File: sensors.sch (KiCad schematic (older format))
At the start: 13 parts, among them Q7 IRLML2502, SW1 TL6215RF200BDT, U13 VL53L0X, U14 APDS-9960

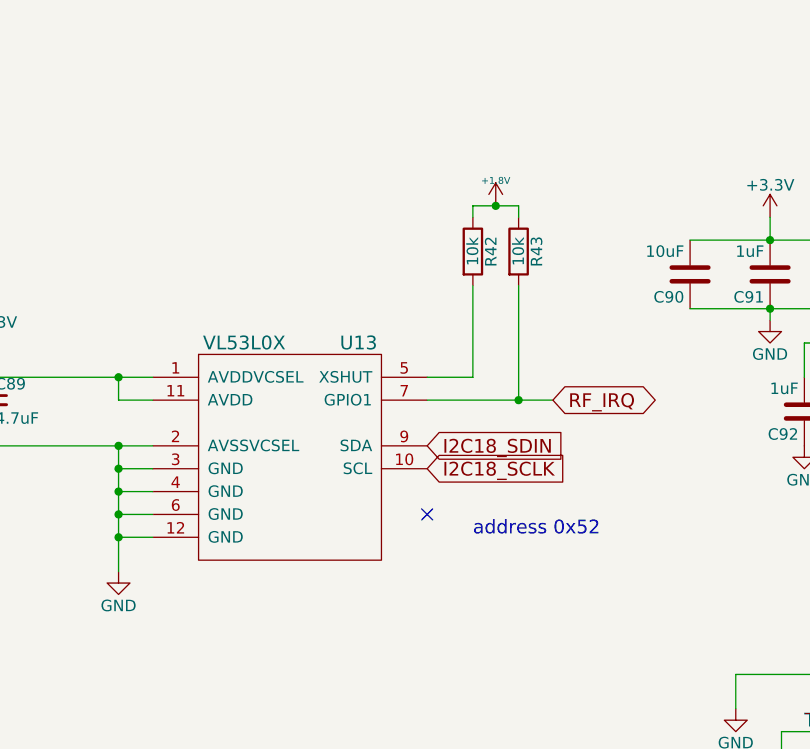
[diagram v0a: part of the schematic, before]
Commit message: added arduino header, shifted components, deleted 50pin ZIF, deleted MIDI in for fear of confusion with headphone jack
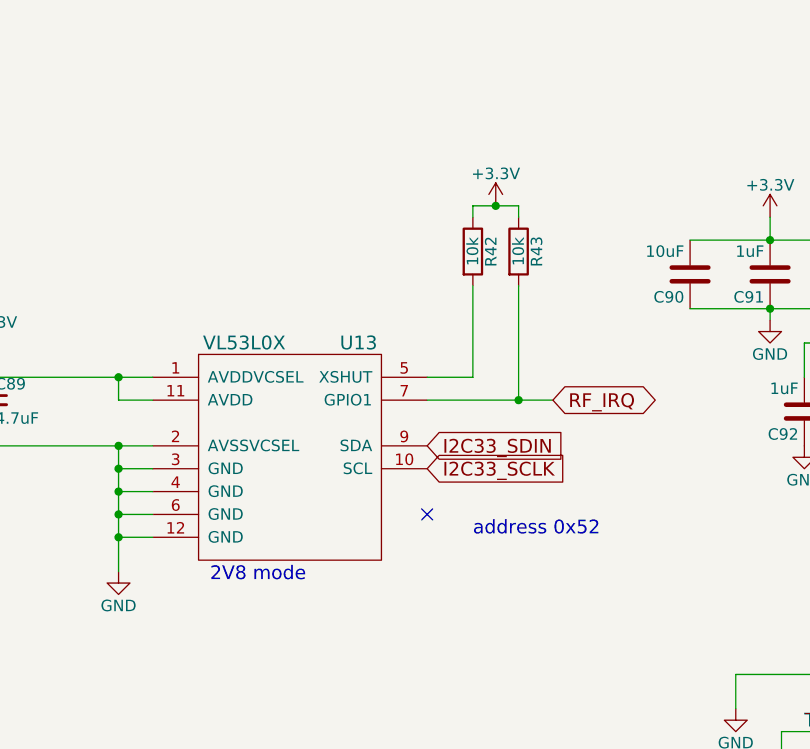
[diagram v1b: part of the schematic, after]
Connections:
- net I2C18_SCLK is gone; now on net I2C33_SCLK: U13.10 (SCL)
- net +1V8: no longer R42.1, R43.1
- net +3V3: now also R42.1, R43.1
- net I2C18_SDIN renamed I2C33_SDIN
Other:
- note added: "2V8 mode"
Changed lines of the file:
@@
-$EndComp
-$Comp
-L power:+1V8 #PWR0141
-U 1 1 585987BD
-P 6200 2550
-F 0 "#PWR0141" H 6200 2690 20  0001 C CNN
-F 1 "+1.8V" H 6200 2660 30  0000 C CNN
-F 2 "" H 6200 2550 60  0001 C CNN
-F 3 "" H 6200 2550 60  0001 C CNN
-	1    6200 2550
-	1    0    0    -1
 $EndComp
 $Comp
@@
 $EndComp
 Text GLabel 5900 3600 2    60   Input ~ 0
-I2C18_SDIN
+I2C33_SDIN
 Text GLabel 5900 3700 2    60   Input ~ 0
-I2C18_SCLK
+I2C33_SCLK
 Text Notes 6100 4000 0    60   ~ 0
 address 0x52
@@
 	6100 2600 6100 2550
 Wire Wire Line
-	6100 2550 6200 2550
-Wire Wire Line
 	6300 2550 6300 2600
 Wire Wire Line
@@
 Connection ~ 4000 3600
 Connection ~ 4550 3300
-Connection ~ 6200 2550
 Wire Wire Line
 	7800 3150 7700 3150
@@
 	4550 3300 4700 3300
 Wire Wire Line
-	6200 2550 6300 2550
-Wire Wire Line
 	7700 3150 7550 3150
 Wire Wire Line
@@
 Text Notes 250  550  0    197  ~ 39
 Sensors
+Text Notes 4950 4200 0    60   ~ 0
+2V8 mode
+Wire Wire Line
+	6100 2550 6200 2550
+$Comp
+L power:+3V3 #PWR0141
+U 1 1 5E2935C0
+P 6200 2550
+F 0 "#PWR0141" H 6200 2400 50  0001 C CNN
+F 1 "+3.3V" H 6200 2690 50  0000 C CNN
+F 2 "" H 6200 2550 50  0000 C CNN
+F 3 "" H 6200 2550 50  0000 C CNN
+	1    6200 2550
+	1    0    0    -1
+$EndComp
+Connection ~ 6200 2550
+Wire Wire Line
+	6200 2550 6300 2550
 $EndSCHEMATC

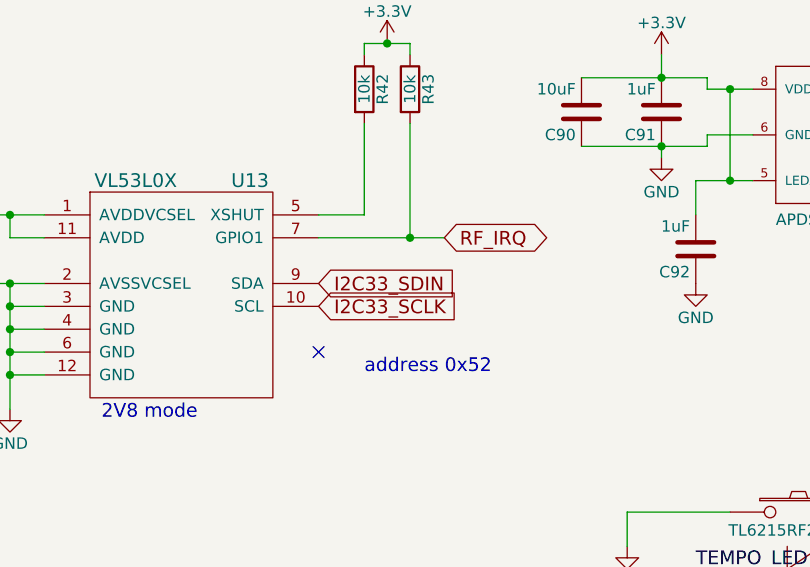
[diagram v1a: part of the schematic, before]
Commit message: routed a few things, about to remove power jack and 5V regulator
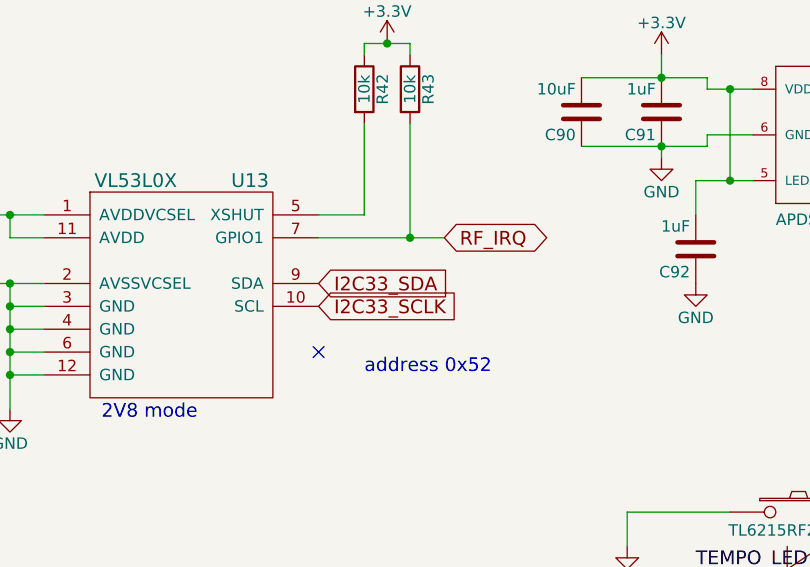
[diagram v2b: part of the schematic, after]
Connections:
- net I2C33_SDIN is gone; now on net I2C33_SDA: U13.9 (SDA)
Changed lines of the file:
@@
 $EndComp
 Text GLabel 5900 3600 2    60   Input ~ 0
-I2C33_SDIN
+I2C33_SDA
 Text GLabel 5900 3700 2    60   Input ~ 0
 I2C33_SCLK

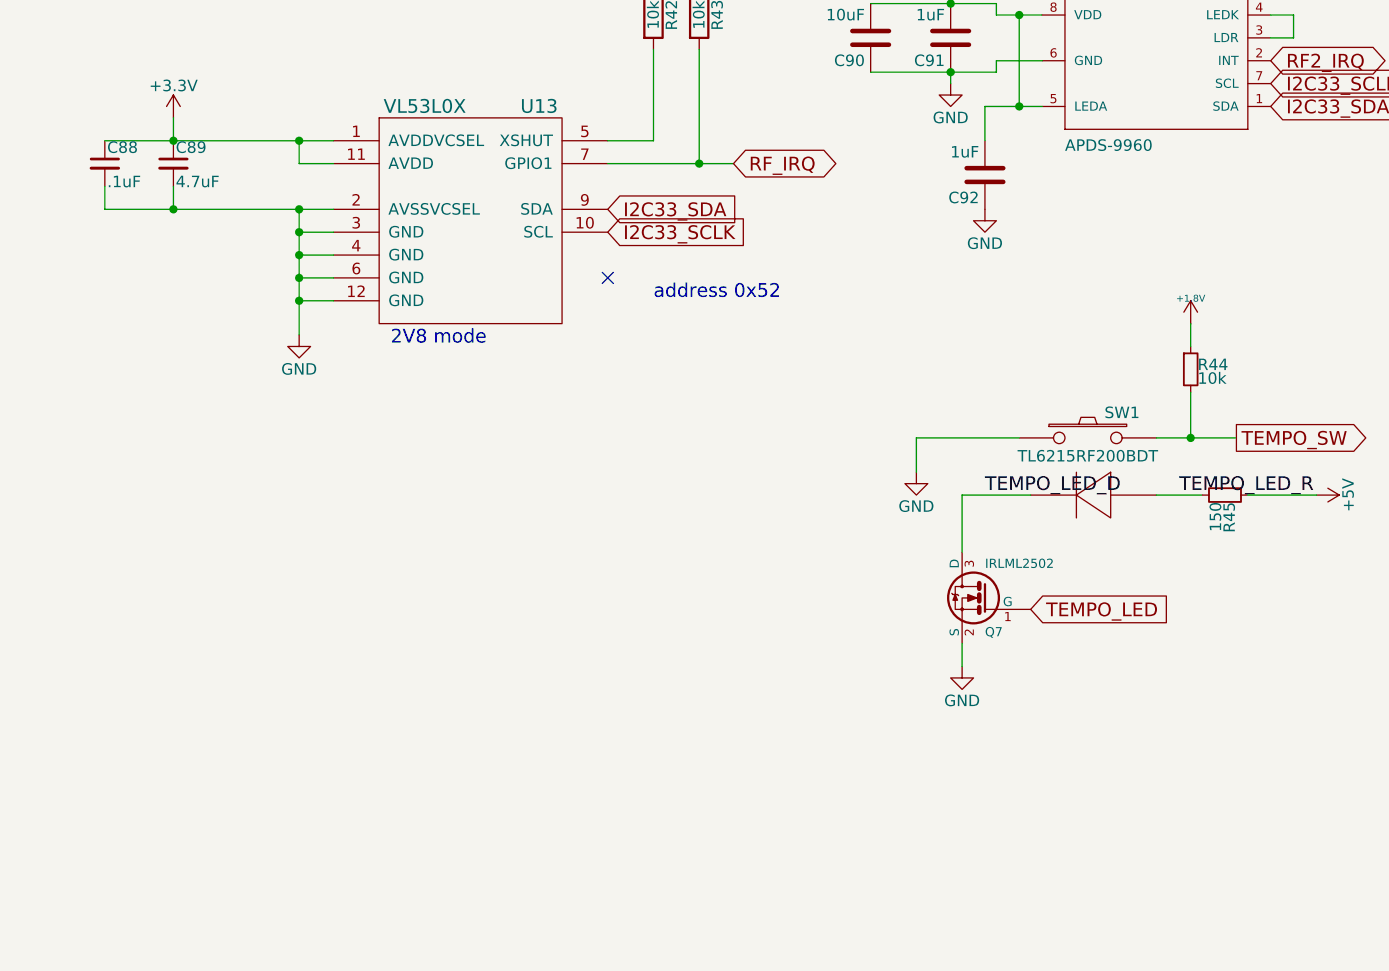
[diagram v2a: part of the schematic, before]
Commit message: length matched important interfaces, added current sense resistors to regulators, about to shrink silkscreen designators
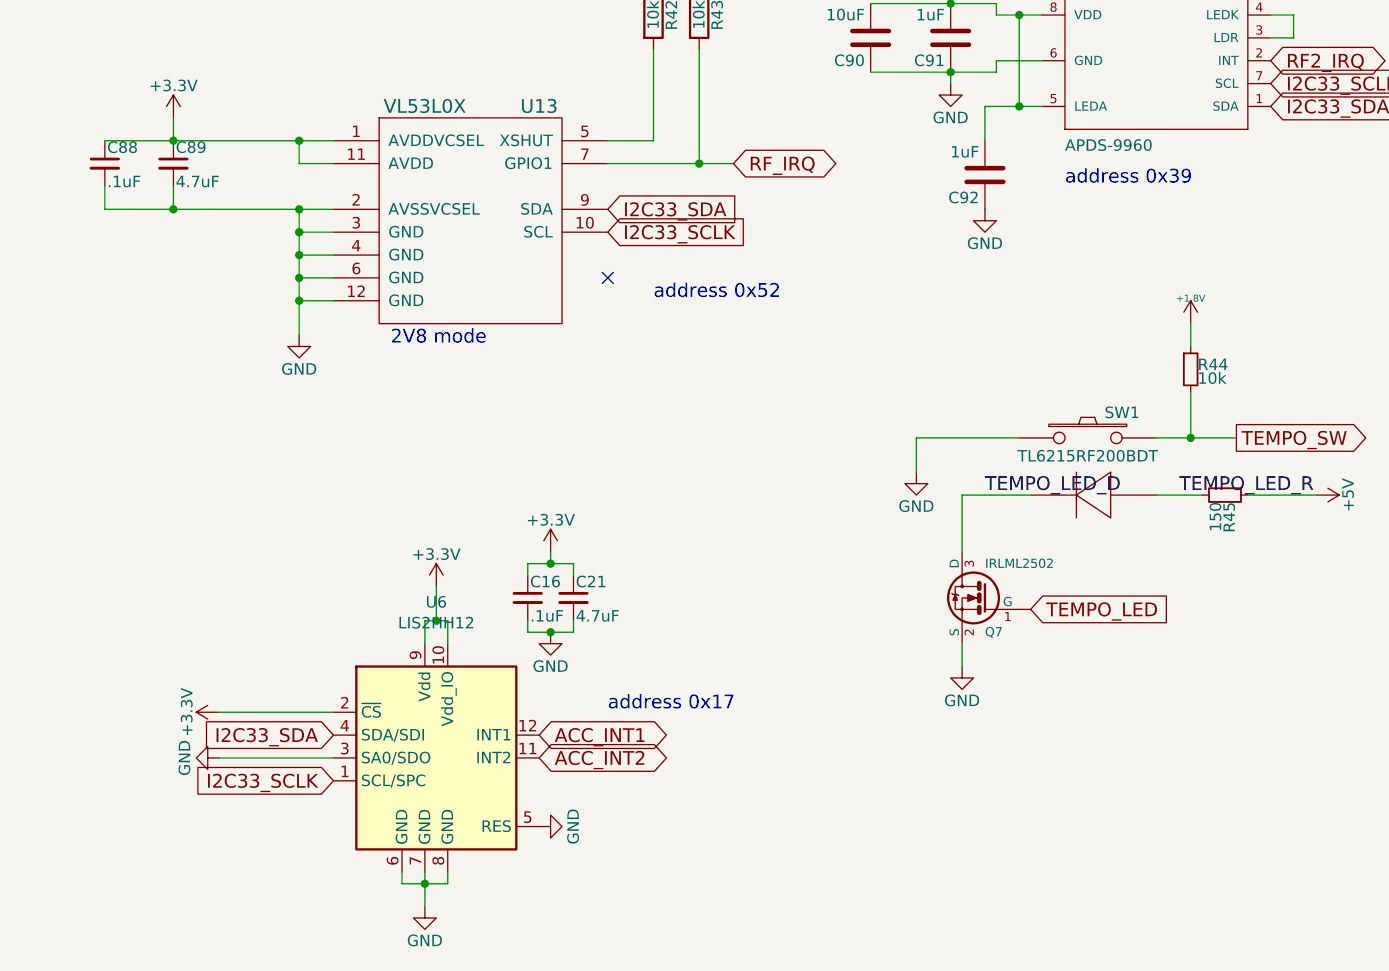
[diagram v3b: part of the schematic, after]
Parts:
- added C16: .1uF, Capacitor_SMD:C_0402_1005Metric, symbol Device:C_Small
- added C21: 4.7uF, Capacitor_SMD:C_0402_1005Metric, symbol Device:C_Small
- added U6: LIS2HH12, Package_LGA:LGA-12_2x2mm_P0.5mm, symbol Sensor_Motion:LIS2HH12
- U14: MFR (none) -> Broadcom Limited; MPN (none) -> APDS-9960; SPN (none) -> 516-3480-1-ND; SPR (none) -> Digikey; SPURL (none) -> -
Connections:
- net +3V3: now also C16.1, C21.1, U6.10 (Vdd_IO), U6.2 (~CS), U6.9 (Vdd)
- net GND: now also C16.2, C21.2, U6.3 (SA0/SDO), U6.5 (RES), U6.6 (GND), U6.7 (GND), U6.8 (GND)
- net I2C33_SCLK: now also U6.1 (SCL/SPC)
- net I2C33_SDA: now also U6.4 (SDA/SDI)
- new net ACC_INT1: U6.12 (INT1)
- new net ACC_INT2: U6.11 (INT2)
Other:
- note added: "address 0x17"
- note added: "address 0x39"

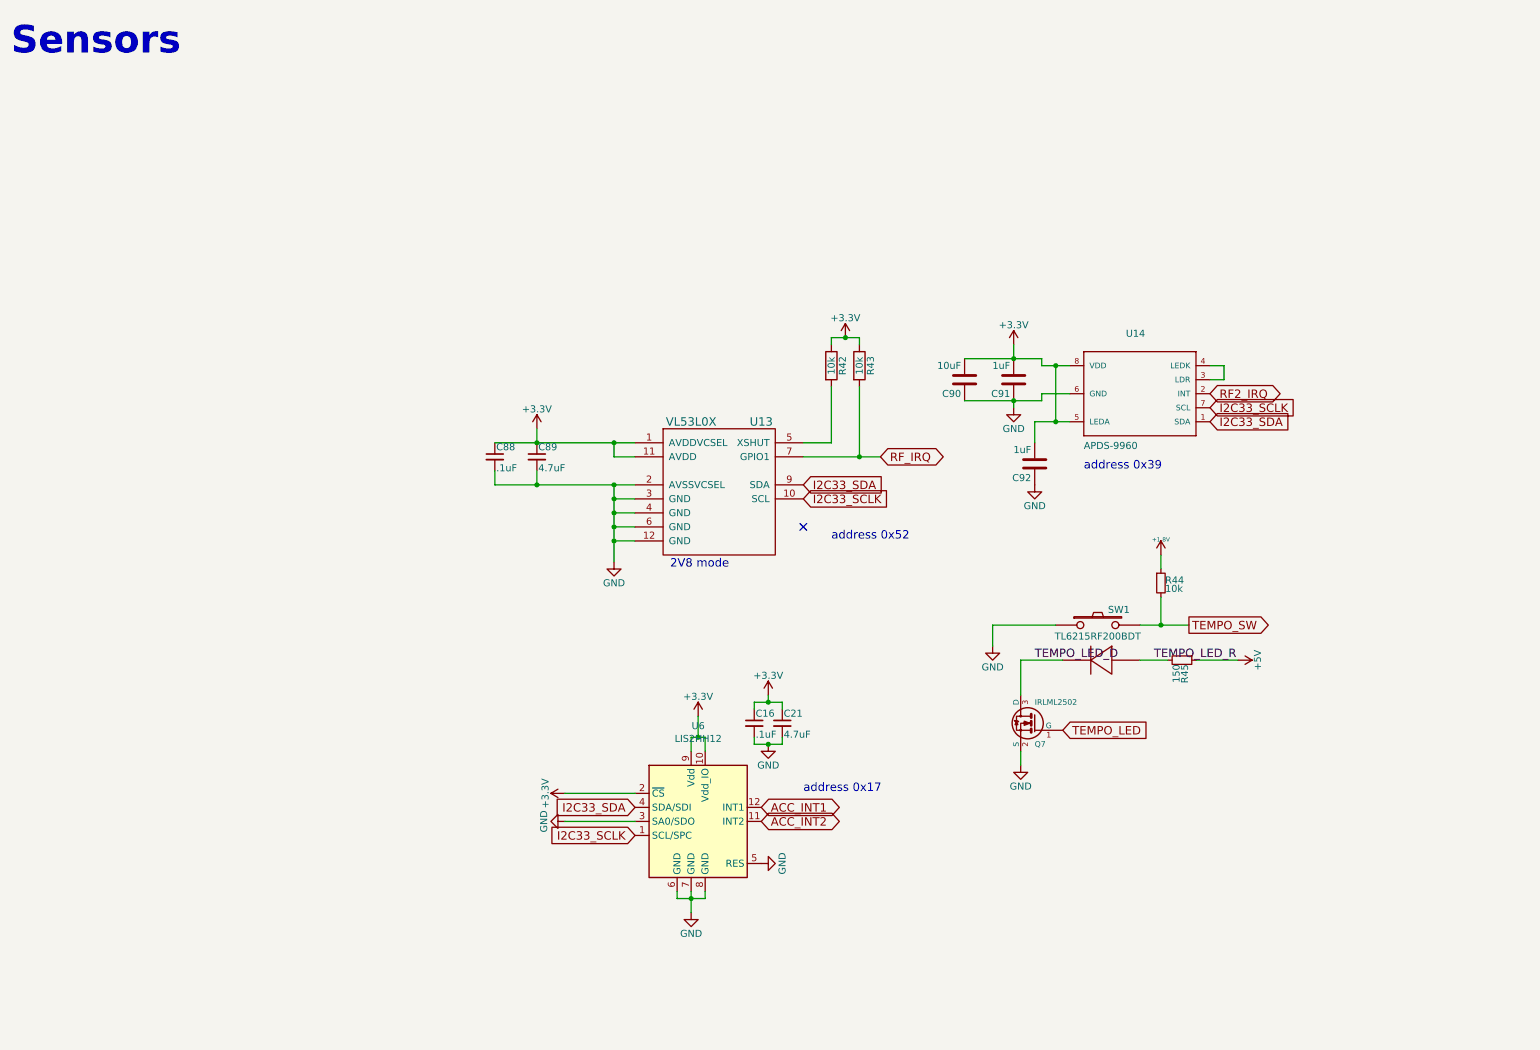
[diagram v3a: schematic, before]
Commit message: finished review with gerber output. still need to relocate rangefinders / LEDs
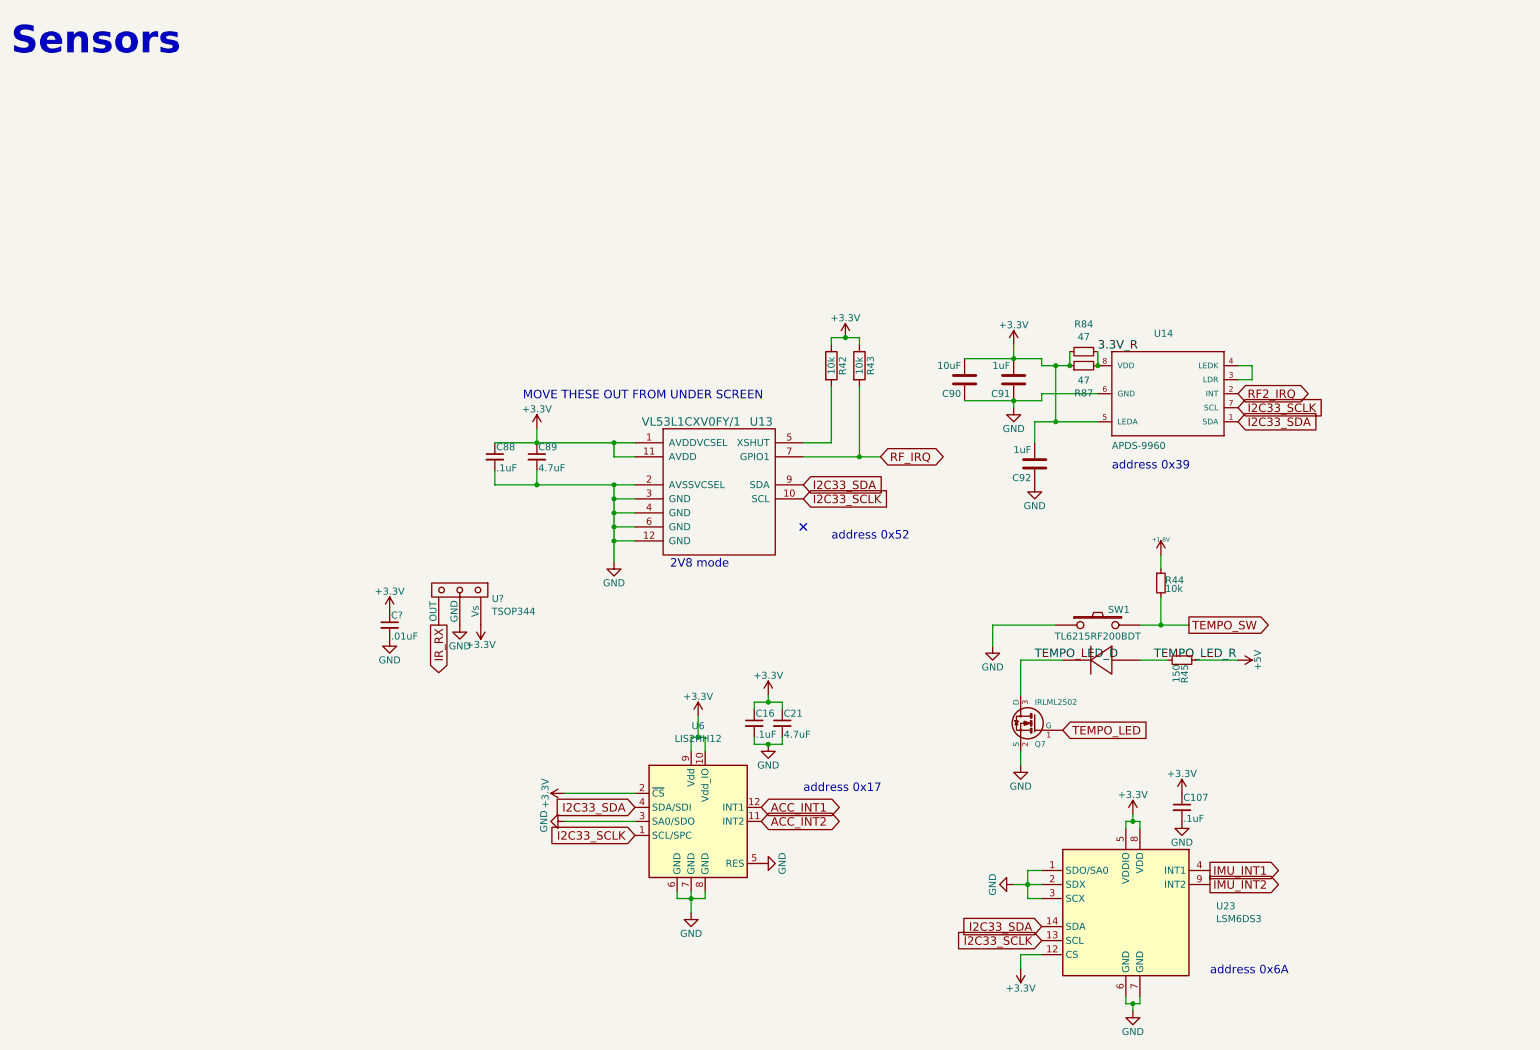
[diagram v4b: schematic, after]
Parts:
- added C107: .1uF, Capacitor_SMD:C_0402_1005Metric, symbol Device:C_Small
- added C?: .01uF, Capacitor_SMD:C_0402_1005Metric, symbol Device:C_Small
- added R84, R87: 47, Resistor_SMD:R_0402_1005Metric, symbol Device:R_Small
- added U23: LSM6DS3, Package_LGA:LGA-14_3x2.5mm_P0.5mm_LayoutBorder3x4y, symbol Sensor_Motion:LSM6DS3
- added U?: TSOP344, DFTcustom:JUMPER_3PIN, symbol DFTCustom:TSOP344
- U13: value VL53L0X -> VL53L1CXV0FY/1; MPN VL53L0CXV0DH/1 -> VL53L1CXV0FY/1; SPN 497-16538-1-ND -> 497-17764-2-ND
- U6: MFR (none) -> STMicroelectronics; MPN (none) -> LIS2HH12TR; SPN (none) -> 497-15069-1-ND; SPR (none) -> Digikey; SPURL (none) -> -
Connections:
- net +3V3: now also C107.1, C?.1, R84.2, R87.1, U23.12 (CS), U23.5 (VDDIO), U23.8 (VDD), U?.3 (Vs); no longer U14.8 (VDD)
- net GND: now also C107.2, C?.2, U23.1 (SDO/SA0), U23.2 (SDX), U23.3 (SCX), U23.6 (GND), U23.7 (GND), U?.2 (GND)
- net I2C33_SCLK: now also U23.13 (SCL)
- net I2C33_SDA: now also U23.14 (SDA)
- new net 3.3V_R: R84.1, R87.2, U14.8 (VDD)
- new net IMU_INT1: U23.4 (INT1)
- new net IMU_INT2: U23.9 (INT2)
- new net IR_RX: U?.1 (OUT)
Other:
- note added: "MOVE THESE OUT FROM UNDER SCREEN"
- note added: "address 0x6A"
- moved on the sheet: U14
